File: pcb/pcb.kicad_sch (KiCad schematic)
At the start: 17 parts, among them J1 OLED, J2 Thermocouple, J3 Interupt, J4 UART, Q1 NPN, Q2 NPN, U2 MAX6675ISA_, U5 WEMOS_D1_mini

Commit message: updated changes in pcb
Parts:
- removed Q2: NPN, Package_TO_SOT_SMD:SOT-23-3, symbol Simulation_SPICE:NPN
- R5: footprint Resistor_THT:R_Axial_DIN0207_L6.3mm_D2.5mm_P10.16mm_Horizontal -> Resistor_SMD:R_1206_3216Metric_Pad1.30x1.75mm_HandSolder
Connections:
- net +5V: no longer R5.2 (-)
- net GND: now also R5.1 (+)
- net at Q1.1 (C): now also BZ1.2; no longer R5.1 (+)
- net at Q1.2 (B), R3.2 (-): now also R5.2 (-)
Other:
- moved on the sheet: BZ1, Q1, R3

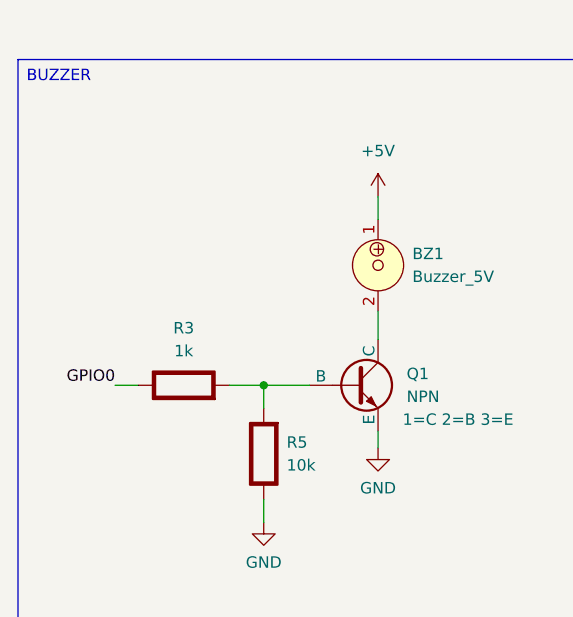
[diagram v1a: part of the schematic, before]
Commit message: added battery functionality, updated pcb
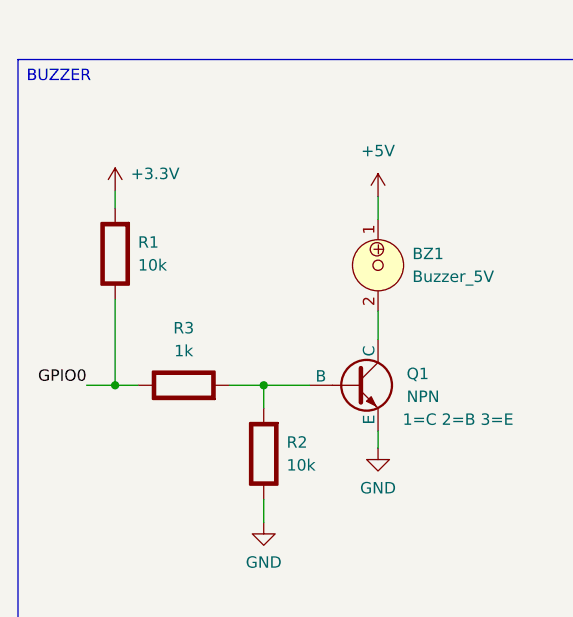
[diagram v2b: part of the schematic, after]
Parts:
- added R1: 10k, Resistor_THT:R_Axial_DIN0207_L6.3mm_D2.5mm_P10.16mm_Horizontal, symbol PCM_Elektuur:R
- renumbered R5 to R2
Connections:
- net +3.3V: now also R1.2 (-)
- net GPIO0: now also R1.1 (+)
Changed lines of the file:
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@@
 		(color 0 0 0 0)
 	)
+	(junction
+		(at 55.88 104.775)
+		(diameter 0)
+		(color 0 0 0 0)
+	)
 	(no_connect
 		(at 156.21 104.14)
@@
 	(wire
 		(pts
-			(xy 55.88 104.775) (xy 58.42 104.775)
+			(xy 52.705 104.775) (xy 55.88 104.775)
 		)
 		(stroke
@@
 	(wire
 		(pts
+			(xy 55.88 104.775) (xy 58.42 104.775)
+		)
+		(stroke
+			(width 0)
+			(type default)
+		)
+	)
+	(wire
+		(pts
 			(xy 233.68 79.375) (xy 233.68 81.28)
 		)
@@
 	(wire
 		(pts
+			(xy 55.88 95.25) (xy 55.88 104.775)
+		)
+		(stroke
+			(width 0)
+			(type default)
+		)
+	)
+	(wire
+		(pts
 			(xy 196.85 54.61) (xy 196.85 55.88)
 		)
@@
 	(wire
 		(pts
+			(xy 55.88 83.185) (xy 55.88 85.09)
+		)
+		(stroke
+			(width 0)
+			(type default)
+		)
+	)
+	(wire
+		(pts
 			(xy 85.09 109.855) (xy 85.09 111.76)
 		)
@@
 	)
 	(label "GPIO0"
-		(at 55.88 104.775 180)
+		(at 52.705 104.775 180)
 		(effects
 			(font
@@
 	)
 	(symbol
+		(lib_id "PCM_Elektuur:R")
+		(at 55.88 90.17 180)
+		(unit 1)
+		(exclude_from_sim no)
+		(in_bom yes)
+		(on_board yes)
+		(dnp no)
+		(fields_autoplaced yes)
+		(property "Reference" "R1"
+			(at 58.42 88.8999 0)
+			(effects
+				(font
+					(size 1.27 1.27)
+				)
+				(justify right)
+			)
+		)
+		(property "Value" "10k"
+			(at 58.42 91.4399 0)
+			(effects
+				(font
+					(size 1.27 1.27)
+				)
+				(justify right)
+			)
+		)
+		(property "Footprint" "Resistor_THT:R_Axial_DIN0207_L6.3mm_D2.5mm_P10.16mm_Horizontal"
+			(at 55.88 90.17 0)
+			(effects
+				(font
+					(size 1.27 1.27)
+				)
+				(hide yes)
+			)
+		)
+		(property "Datasheet" ""
+			(at 55.88 90.17 0)
+			(effects
+				(font
+					(size 1.27 1.27)
+				)
+				(hide yes)
+			)
+		)
+		(property "Description" "resistor"
+			(at 55.88 90.17 0)
+			(effects
+				(font
+					(size 1.27 1.27)
+				)
+				(hide yes)
+			)
+		)
+		(property "Indicator" "+"
+			(at 59.055 93.345 0)
+			(effects
+				(font
+					(size 1.27 1.27)
+				)
+				(hide yes)
+			)
+		)
+		(property "Rating" "W"
+			(at 53.34 86.995 0)
+			(effects
+				(font
+					(size 1.27 1.27)
+				)
+				(justify left)
+				(hide yes)
+			)
+		)
+		(pin "2"
+		)
+		(pin "1"
+		)
+		(instances
+			(project "pcb"
+				(path "/32d2d8e4-ddd7-43e3-8a2d-1c60906095aa"
+					(reference "R1")
+					(unit 1)
+				)
+			)
+		)
+	)
+	(symbol
 		(lib_id "RF_Module:WEMOS_D1_mini")
 		(at 236.22 101.6 0)
@@
 		(dnp no)
 		(fields_autoplaced yes)
-		(property "Reference" "R5"
+		(property "Reference" "R2"
 			(at 74.93 111.1249 0)
 			(effects
@@
 			(project "pcb"
 				(path "/32d2d8e4-ddd7-43e3-8a2d-1c60906095aa"
-					(reference "R5")
+					(reference "R2")
 					(unit 1)
 				)
@@
 					(unit 1)
 				)
+			)
+		)
+	)
+	(symbol
+		(lib_id "power:+3.3V")
+		(at 55.88 83.185 0)
+		(unit 1)
+		(exclude_from_sim no)
+		(in_bom yes)
+		(on_board yes)
+		(dnp no)
+		(property "Reference" "#PWR028"
+			(at 55.88 86.995 0)
+			(effects
+				(font
+					(size 1.27 1.27)
+				)
+				(hide yes)
+			)
+		)
+		(property "Value" "+3.3V"
+			(at 60.325 81.28 0)
+			(effects
+				(font
+					(size 1.27 1.27)
+				)
+			)
+		)
+		(property "Footprint" ""
+			(at 55.88 83.185 0)
+			(effects
+				(font
+					(size 1.27 1.27)
+				)
+				(hide yes)
+			)
+		)
+		(property "Datasheet" ""
+			(at 55.88 83.185 0)
+			(effects
+				(font
+					(size 1.27 1.27)
+				)
+				(hide yes)
+			)
+		)
+		(property "Description" "Power symbol creates a global label with name \"+3.3V\""
+			(at 55.88 83.185 0)
+			(effects
+				(font
+					(size 1.27 1.27)
+				)
+				(hide yes)
+			)
+		)
+		(pin "1"
+		)
+		(instances
+			(project "pcb"
+				(path "/32d2d8e4-ddd7-43e3-8a2d-1c60906095aa"
+					(reference "#PWR028")
+					(unit 1)
+				)
